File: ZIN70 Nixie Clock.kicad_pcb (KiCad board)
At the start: 2 copper layers, 270 x 90 mm, 43 parts, among them U1 HV5122, U2 HV5122, U3 CD40109BPW

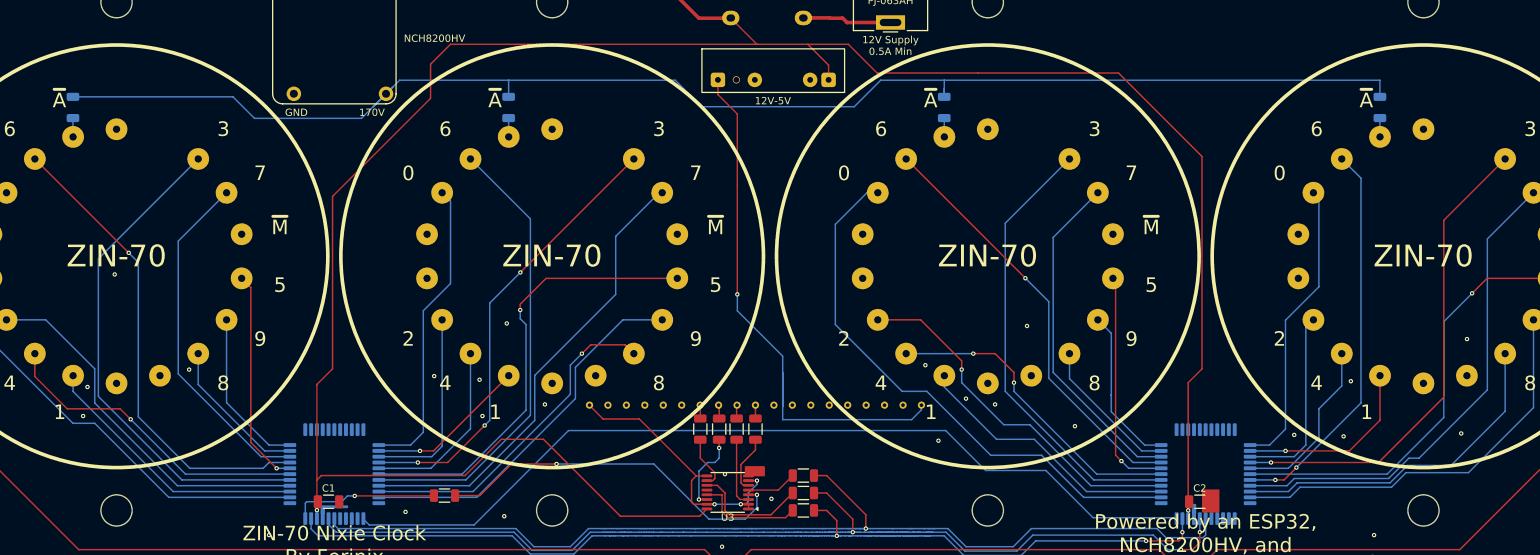
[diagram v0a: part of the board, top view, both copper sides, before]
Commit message: Update the clock with 5mm indicators
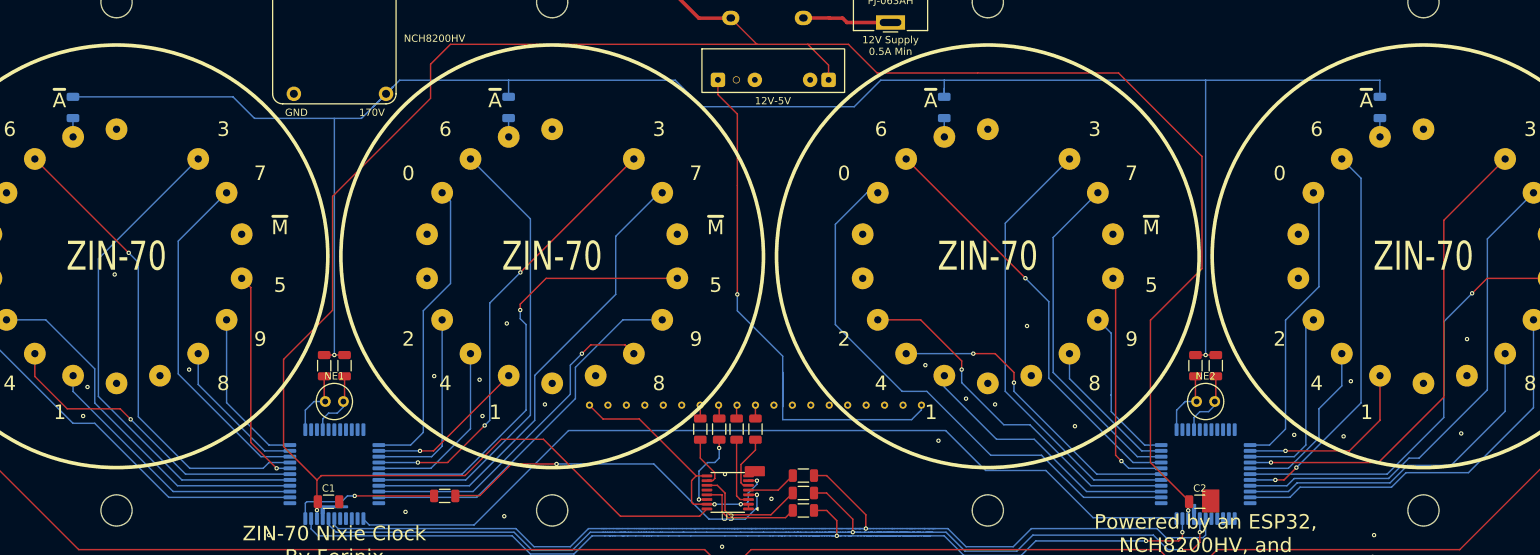
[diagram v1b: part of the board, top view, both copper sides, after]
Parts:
- added NE1: NE-2, NixFootprints:NE-2_5mm, F.Cu at (130.0, 120.0)
- added NE2: NE-2, NixFootprints:NE-2_5mm, F.Cu at (250.0, 120.0)
- added R10: 1K, Resistor_SMD:R_1206_3216Metric, F.Cu at (194.6, 132.6)
- added R11: 1K, Resistor_SMD:R_1206_3216Metric, F.Cu at (194.6, 130.2)
- added R12: 1K, Resistor_SMD:R_1206_3216Metric, F.Cu at (145.2, 133.0)
- added R9: 1K, Resistor_SMD:R_1206_3216Metric, F.Cu at (194.6, 135.0)
- R5, R6, R7, R8: value 1K -> 100K
- moved R6 65.0 mm to (131.4, 115.1), turned to 90 degrees
- moved R8 60.2 mm to (251.4, 115.1), turned to 90 degrees
- moved R7 56.8 mm to (248.6, 115.1), turned to 90 degrees
- moved R5 24.4 mm to (128.6, 115.1), turned to 90 degrees
- renumbered ZIN-70 to NIX1, ZIN-70 to NIX2, ZIN-70 to NIX3, ZIN-70 to NIX4, R9 to R13, R10 to R14, R11 to R15, R12 to R16
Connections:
- R5 pad 1: Net-(U1-DIN) -> Net-(U1-HV11)
- R5 pad 2: Net-(U3-E) -> +170V
- R6 pad 1: Net-(U1-~{OE}) -> Net-(U1-HV14)
- R6 pad 2: Net-(U3-F) -> +170V
- R7 pad 1: Net-(U1-CLK) -> Net-(U2-HV11)
- R7 pad 2: Net-(U3-G) -> +170V
- R8 pad 1: Net-(U1-STR) -> Net-(U2-HV14)
- R8 pad 2: Net-(U3-H) -> +170V
- U1 pad 1: unconnected-(U1-HV11-Pad1) -> Net-(U1-HV11)
- U1 pad 4: unconnected-(U1-HV14-Pad4) -> Net-(U1-HV14)
- U2 pad 1: unconnected-(U2-HV11-Pad1) -> Net-(U2-HV11)
- U2 pad 4: unconnected-(U2-HV14-Pad4) -> Net-(U2-HV14)
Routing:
- net +170V: track 194.9 -> 270.9 mm, vias 0 -> 2
- net Net-(U2-HV14): track 0.00 -> 9.52 mm
- net Net-(U2-HV11): track 0.00 -> 9.48 mm
- net Net-(U1-HV11): track 0.00 -> 9.48 mm
- net Net-(U1-HV14): track 0.00 -> 9.32 mm
- net +12V: track 369.9 -> 378.0 mm

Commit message: Major changes to design
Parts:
- removed the REF** at (188.0, 132.0)
- removed the REF** at (190.4, 75.7)
- added 9V Socket: 9V Socket Slim, NixFootprints:9V Socket Slim, B.Cu at (130.0, 63.8)
- added 9V Socket: 9V Socket Slim, NixFootprints:9V Socket Slim, B.Cu at (250.0, 63.8)
- added REF**: PinHeader_1x03_P2.54mm_Vertical, Connector_PinHeader_2.54mm:PinHeader_1x03_P2.54mm_Vertical, B.Cu at (187.4, 78.0)
- added REF**: RP2040-Tiny Package, NixFootprints:RP2040-Tiny Package, B.Cu at (190.0, 125.0)
- added REF**: PinHeader_1x03_P2.54mm_Vertical, Connector_PinHeader_2.54mm:PinHeader_1x03_P2.54mm_Vertical, F.Cu at (261.5, 67.0)
- R1, R2, R3, R4: value R -> 6.8K
- R5, R6, R7, R8: value 100K -> 200K
- moved G*** 18.6 mm to (245.3, 81.4)
- moved R10 10.0 mm to (204.6, 132.6)
- moved R11 10.0 mm to (204.6, 130.2)
- moved R9 10.0 mm to (204.6, 135.0)
- moved R13 5.82 mm to (191.2, 123.8)
- moved R14 5.82 mm to (193.8, 123.8)
- moved R15 5.82 mm to (186.2, 123.8)
- moved R16 5.82 mm to (188.8, 123.8)
- moved U3 5.82 mm to (190.0, 132.5)
- moved PJ-063AH 0.60 mm to (206.6, 67.2)
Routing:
- net +12V: track 378.0 -> 573.4 mm
- net +5V: track 0.00 -> 65.4 mm
- net (no net): track 308.1 -> 261.9 mm, vias 1 -> 2
- net +3.3V: track 38.4 -> 22.8 mm
- net Net-(U3-E): track 50.1 -> 57.0 mm
- net CLK: track 1.94 -> 8.08 mm
- net EN: track 1.94 -> 8.04 mm
- net DIN: track 1.94 -> 8.04 mm
- net STR: track 1.94 -> 8.01 mm
- net Net-(U3-H): track 14.9 -> 19.6 mm
- net Net-(U3-F): track 6.93 -> 11.1 mm
- net Net-(U3-G): track 16.2 -> 20.3 mm
- net +170V: track 270.9 -> 267.9 mm
- net Net-(NIX3-0): track 76.2 -> 75.4 mm
- net GND: vias 29 -> 33
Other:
- board text added: "12V to 5V"
- board text added: "Powered by an RP2040, NCH8200HV, and HV5122s"
- board text removed: "Powered by an ESP32, NCH8200HV, and HV5122s"
